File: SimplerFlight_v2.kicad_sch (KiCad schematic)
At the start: 19 parts, among them J2 Conn_01x04_Pin, J3 Conn_01x04_Pin, J4 Conn_01x04_Pin, J5 Conn_01x04_Pin, SW1 SW_SPDT, U2 STM32F401RETx, Y1 16MHz

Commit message: Commit
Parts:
- removed C1: 10uF, Capacitor_SMD:C_0805_2012Metric, symbol Device:C
- removed C10, C11: 10pF, Capacitor_SMD:C_0805_2012Metric, symbol Device:C
- removed C2, C3, C4, C5, C6, C9: 100nF, Capacitor_SMD:C_0805_2012Metric, symbol Device:C
- removed J2, J3, J4, J5: Conn_01x04_Pin, Connector_PinHeader_2.54mm:PinHeader_1x04_P2.54mm_Vertical, symbol Connector:Conn_01x04_Pin
- removed R2: 10k, Capacitor_SMD:C_0805_2012Metric, symbol Device:R
- removed R3, R4: 1k5, Capacitor_SMD:C_0805_2012Metric, symbol Device:R
- removed SW1: SW_SPDT, Button_Switch_SMD:SW_SPDT_PCM12, symbol Switch:SW_SPDT
- removed U2: STM32F401RETx, Package_QFP:LQFP-64_10x10mm_P0.5mm, symbol MCU_ST_STM32F4:STM32F401RETx
- removed Y1: 16MHz, Crystal:Crystal_SMD_3225-4Pin_3.2x2.5mm, symbol Device:Crystal_GND24
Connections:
- no-connect marks 39 -> 0
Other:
- removed sheet Mounting Holes
- added sheet Microcontroller (microcontroller.kicad_sch)
- note removed: "Capacitor Load = 2 * (CL0 - Cs) = 2 * (10 - 5) = 10 pF"
- note removed: "See: AN2867"
- note removed: "x1 100nF per VDD Pin"

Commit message: addecd stuff
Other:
- added sheet Peripherals (peripherals.kicad_sch)
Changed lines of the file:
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@@
+			"AAAAAAAAAAAAAAAAAAAAAAAAAAAAAAAAAAAAAAAAAAAAAAAAAAAAAAAAAAAAAAAAAAAAAAAAAAAA"
+			"AAAAAAAAAAAAAAAAAAAAAAAAAAAAAAAAAAAAAAAAAAAAAAAAAAAAAAAAAAAAAAAAAAAAAAAAAAAA"
+			"AAAAAAAAAAAAAAAAAAAAAAAAAAAAAAAAAAAAAAAAAAAAAAAAAAAAAAAAAAAAAAAAAAAAAAAAAAAA"
+			"AAAAAAAAAAAAAAAAAAAAAAAAAAAAAAAAAAAAAAAAAAAAAAAAAAAAAAAAAAAAAAAAAAAAAAAAAAAA"
+			"AAAAAAAAAAAAAAAAAAAAAAAAAAAAAAAAAAAAAAAAAAAAAAAAAAAAAAAAAAAAAAAAAAAAAAAAAAAA"
+			"AAAAAAAAAAAAAAAAAAAAAAAAAAAAAAAAAAAAAAAAAAAAAAAAAAAAAAAAAAAAAAAAAAAAAAAAAAAA"
+			"AAAAAAAAAAAAAAAAAAAAAAAAAAAAAAAAAAAAAAAAAAAAAAAAAAAAAAAAAAAAAAAAAAAAAAAAAAAA"
+			"AAAAAAAAAAAAAAAAAAAAAAAAAAAAAAAAAAAAAAAAAAAAAAAAAAAAAAAAAAAAAAAAAAAAAAAAAAAA"
+			"AAAAAAAAAAAAAAAAAAAAAAAAAAAAAAAAAAAAAAAAAAAAAAAAAAAAAAAAAAAAAAAAAAAAAAAAAAAA"
+			"AAAAAAAAAAAAAAAAAAAAAAAAAAAAAAAAAAAAAAAAAAAAAAAAAAAAAAAAAAAAAAAAAAAAAAAAAAAA"
+			"AAAAAAAAAAAAAAAAAAAAAAAAAAAAAAAAAAAAAAAAAAAAAAAAAAAAAAAAAAAAAAAAAAAAAAAAAAAA"
+			"AAAAAAAAAAAAAAAAAAAAAAAAAAAAAAAAAAAAAAAAAAAAAAAAAAAAAAAAAAAAAAAAAAAAAAAAAAAA"
+			"AAAAAAAAAAAAAAAAAAAAAAAAAAAAAAAAAAAAAAAAAAAAAAAAAAAAAAAAAAAAAAAAAAAAAAAAAAAA"
+			"AAAAAAAAAAAAAAAAAAAAAAAAAAAAAAAAAAAAAAAAAAAAAAAAAAAAAAAAAAAAAAAAAAAAAAAAAAAA"
+			"AAAAAAAAAAAAAAAAAAAAAAAAAAAAAAAAAAAAAAAAAAAAAAAAAAAAAAAAAAAAAAAAAAAAAAAAAAAA"
+			"AAAAAAAAAAAAAAAAAAAAAAAAAAAAAAAAAAAAAAAAAAAAAAAAAAAAAAAAAAAAAAAAAAAAAAAAAAAA"
+			"AAAAAAAAAAAAAAAAAAAAAAAAAAAAAAAAAAAAAAAAAAAAAAAAAAAAAAAAAAAAAAAAAAAAAAAAAAAA"
+			"AAAAAAAAAAAAAAAAAAAAAAAAAAAAAAAAAAAAAAAAAAAAAAAAAAAAAAAAAAAAAAAAAAAAAAAAAAAA"
 			"AAAAAAAAAAAAAAAAAAAAAAAAAAAAAAAAAAAAAAAAAAAAAAAAAAAAAAAAAAAAAAAAAAAAAAAAAAAA"
 			"AAAAAAAAAAAAAAAAAAAAAAAAAAAAAAAAAAAAAAAAAAAAAAAAAAAAAAAAAAAAAAAAAAAAAAAAAAAA"
@@
 		)
 	)
+	(sheet
+		(at 82.55 72.39)
+		(size 26.67 19.05)
+		(exclude_from_sim no)
+		(in_bom yes)
+		(on_board yes)
+		(dnp no)
+		(fields_autoplaced yes)
+		(stroke
+			(width 0.1524)
+			(type solid)
+		)
+		(fill
+			(color 0 0 0 0.0000)
+		)
+		(property "Sheetname" "Peripherals"
+			(at 82.55 71.6784 0)
+			(effects
+				(font
+					(size 1.27 1.27)
+				)
+				(justify left bottom)
+			)
+		)
+		(property "Sheetfile" "peripherals.kicad_sch"
+			(at 82.55 92.0246 0)
+			(effects
+				(font
+					(size 1.27 1.27)
+				)
+				(justify left top)
+				(hide yes)
+			)
+		)
+		(instances
+			(project "SimplerFlight_v2"
+				(path "/05521696-5bcb-4d0e-9e87-bbc993e58ce4"
+					(page "6")
+				)
+			)
+		)
+	)

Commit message: Updated schematics
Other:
- note added: "CAS Board 2025"
- note removed: "Simpler Flight v2"

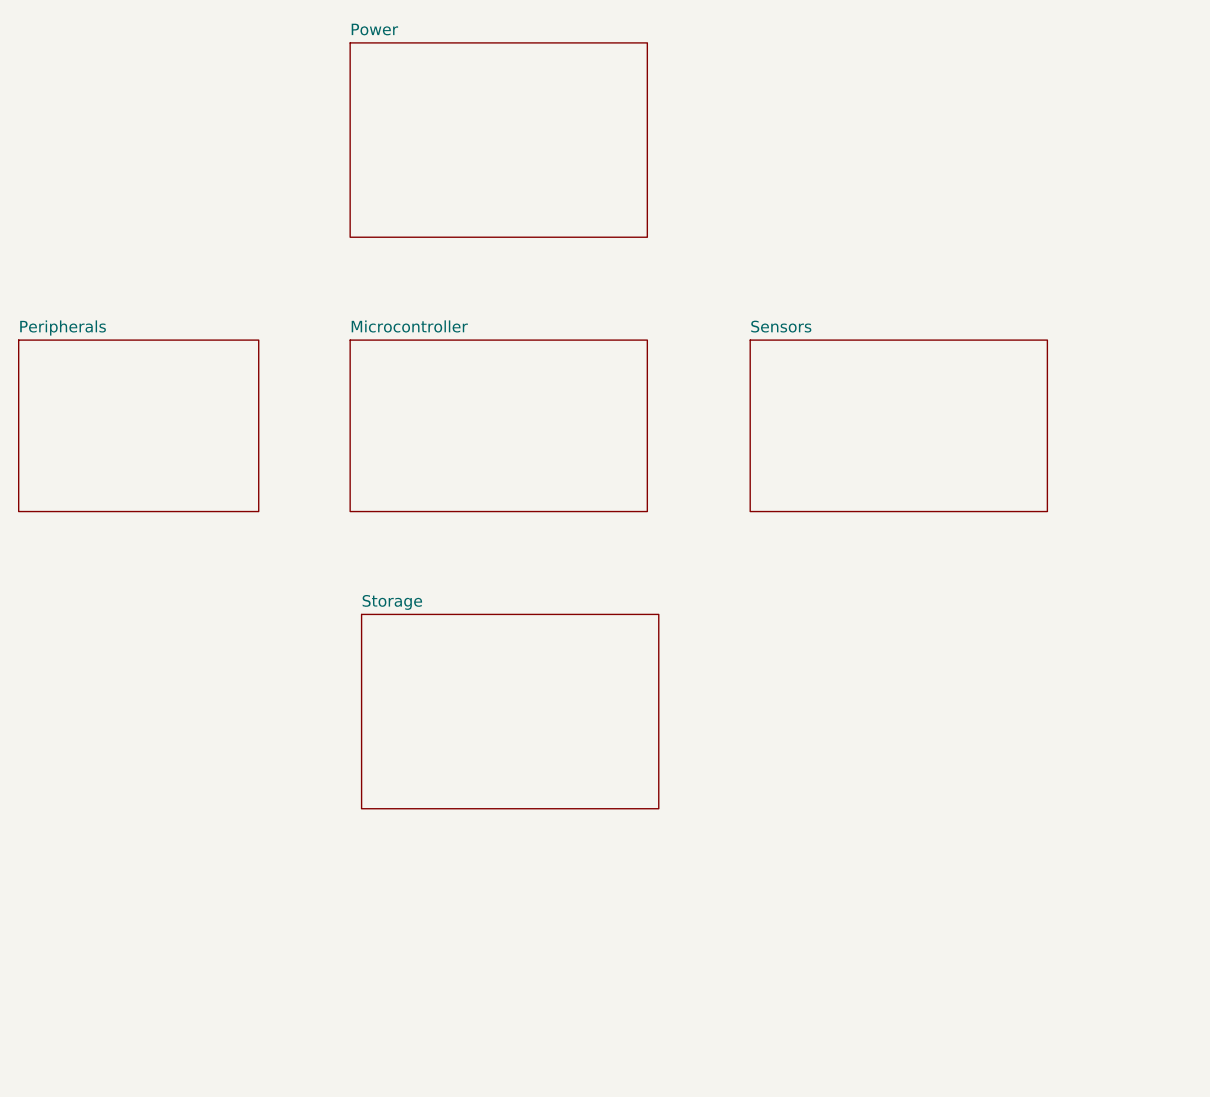
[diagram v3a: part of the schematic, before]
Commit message: Use heirarchical labels
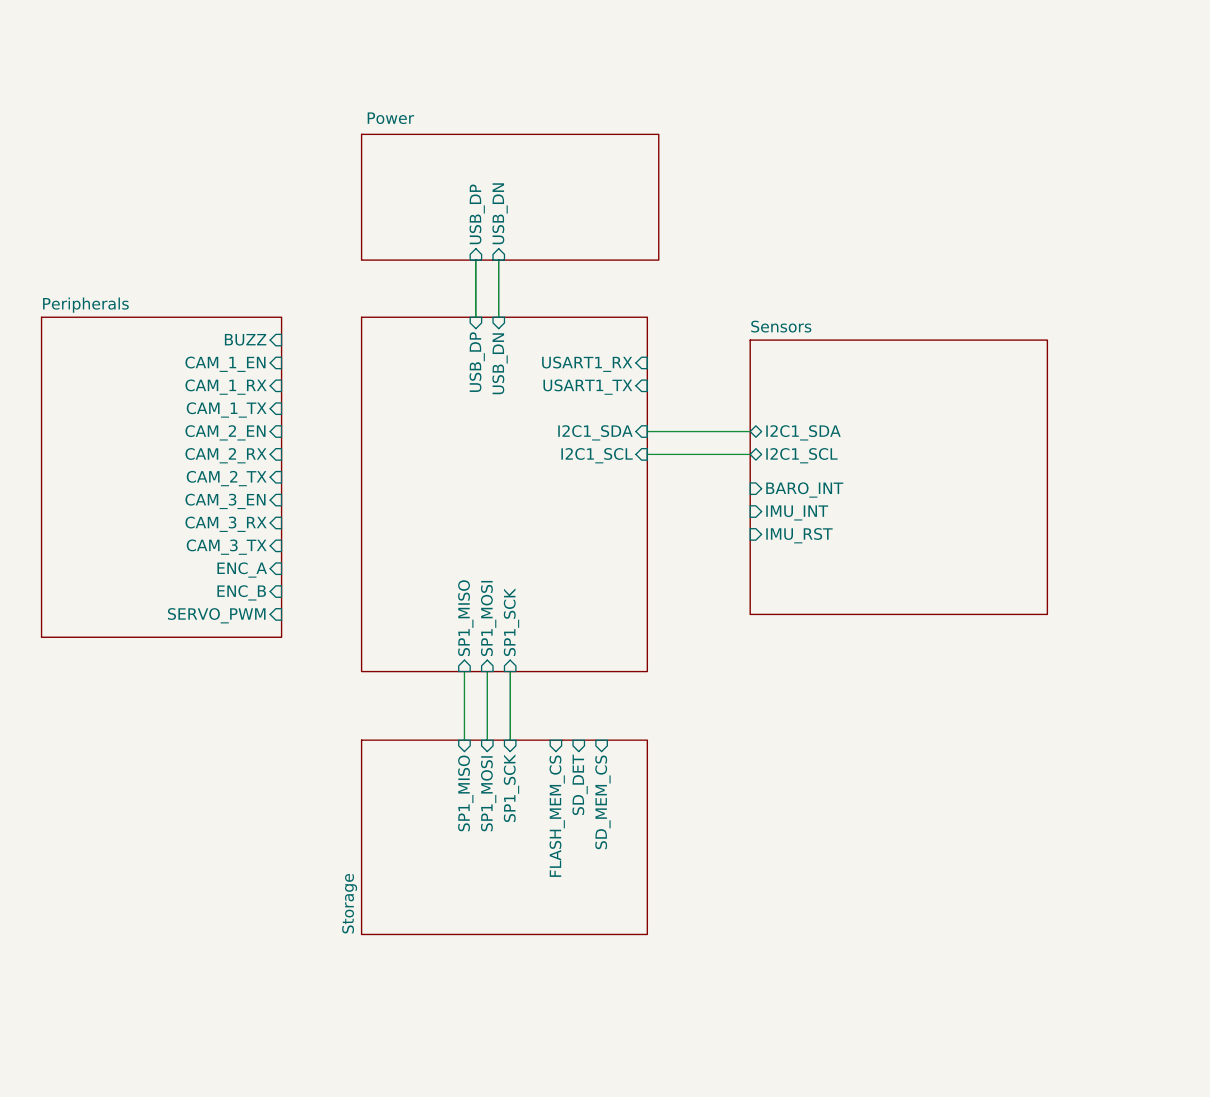
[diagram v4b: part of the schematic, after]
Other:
- sheet Microcontroller ports: added I2C1_SCL, I2C1_SDA, SP1_MISO, SP1_MOSI, SP1_SCK, USART1_RX, USART1_TX, USB_DN, USB_DP; removed none
- sheet Peripherals ports: added BUZZ, CAM_1_EN, CAM_1_RX, CAM_1_TX, CAM_2_EN, CAM_2_RX, CAM_2_TX, CAM_3_EN, CAM_3_RX, CAM_3_TX, ENC_A, ENC_B, SERVO_PWM; removed none
- sheet Power ports: added USB_DN, USB_DP; removed none
- sheet Sensors ports: added BARO_INT, I2C1_SCL, I2C1_SDA, IMU_INT, IMU_RST; removed none
- sheet Storage ports: added FLASH_MEM_CS, SD_DET, SD_MEM_CS, SP1_MISO, SP1_MOSI, SP1_SCK; removed none
